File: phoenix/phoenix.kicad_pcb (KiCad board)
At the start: 2 copper layers, 62.7 x 22.6 mm, 2 parts, among them U1 ATMEGA328P-AU

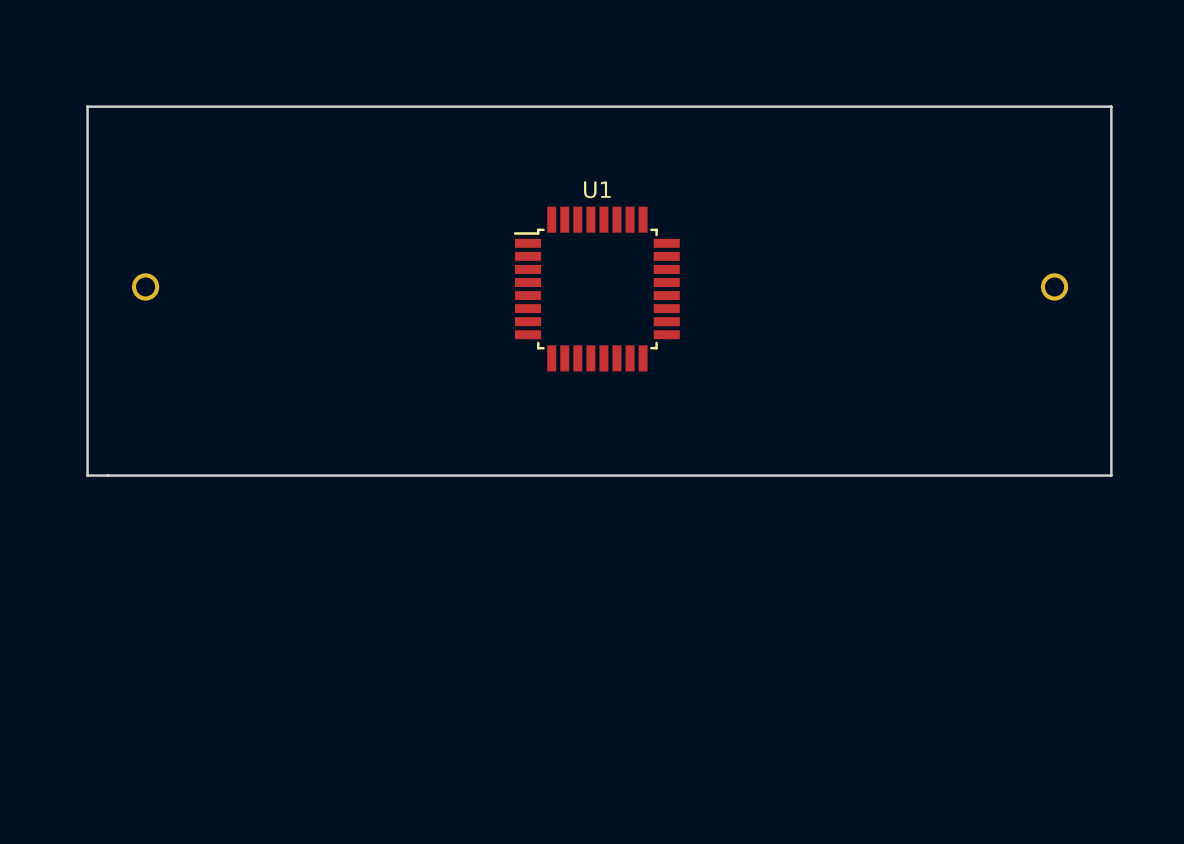
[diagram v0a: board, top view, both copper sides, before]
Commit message: Started layout
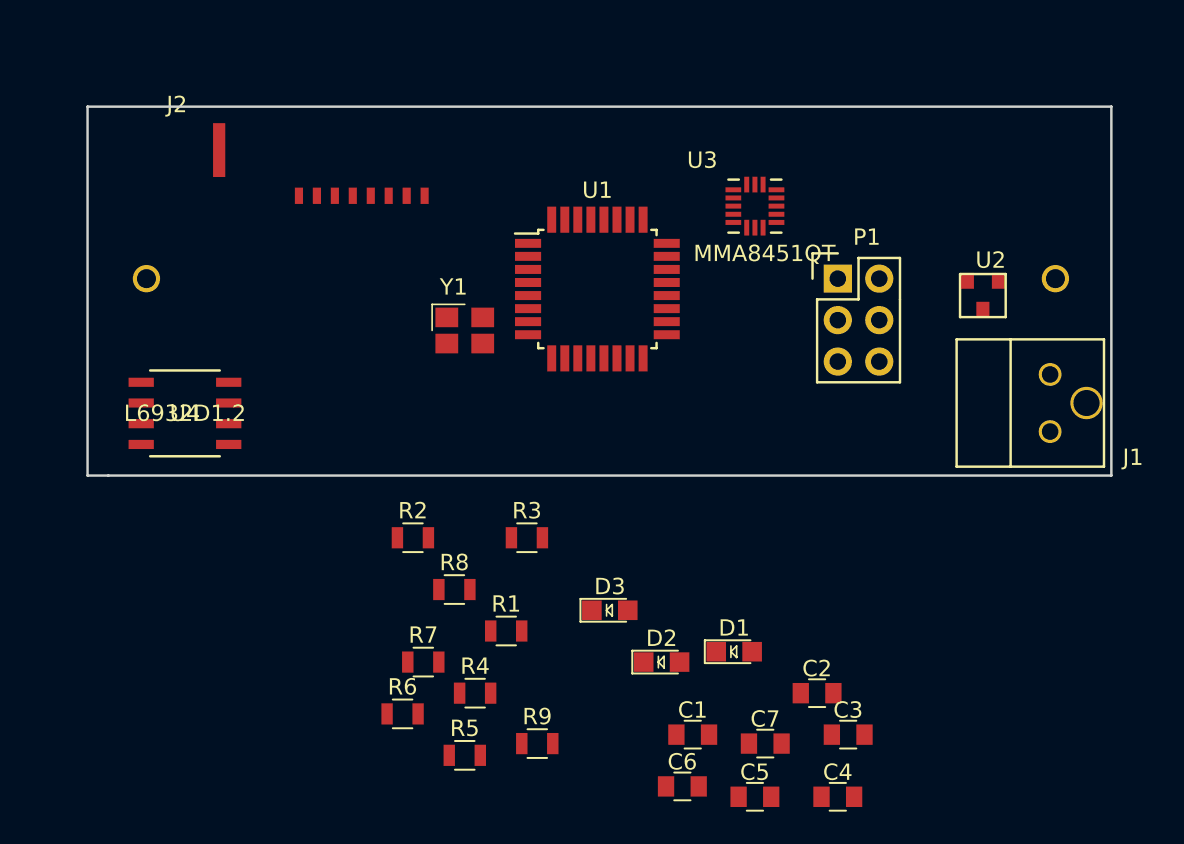
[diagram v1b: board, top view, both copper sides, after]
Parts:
- removed REF**: battery_holder, rocketry:battery_holder
- added BT1: 3.7V Lipo, rocketry:battery_holder, B.Cu at (112.6, 64.1)
- added C1: C_0.1uF, footprints:C_0805_OEM, F.Cu at (146.1, 92.1)
- added C2: C_0.1uF, footprints:C_0805_OEM, F.Cu at (153.7, 89.5)
- added C3: C_10uF, footprints:C_0805_OEM, F.Cu at (155.6, 92.1)
- added C4: C_10uF, footprints:C_0805_OEM, F.Cu at (154.9, 95.9)
- added C5: C_100pF, footprints:C_0805_OEM, F.Cu at (149.9, 95.9)
- added C6: C_30pF, footprints:C_0805_OEM, F.Cu at (145.4, 95.2)
- added C7: C_30pF, footprints:C_0805_OEM, F.Cu at (150.5, 92.6)
- added D1: LED_0805, footprints:LED_0805_OEM, F.Cu at (148.6, 87.0)
- added D2: LED_0805, footprints:LED_0805_OEM, F.Cu at (144.1, 87.6)
- added D3: LED_0805, footprints:LED_0805_OEM, F.Cu at (141.0, 84.5)
- added J1: Ultrafit_2, footprints:Ultrafit_2, F.Cu at (167.9, 70.0)
- added J2: Micro_SD_Card_Det, rocketry:SD-Card, F.Cu at (116.7, 54.6)
- added P1: CONN_02X03, footprints:Pin_Header_Straight_2x03, F.Cu at (154.9, 64.1)
- added R1: R_10k, footprints:R_0805_OEM, F.Cu at (134.6, 85.7)
- added R2: 9K, rocketry:R_0805_OEM, F.Cu at (128.9, 80.0)
- added R3: 5K, rocketry:R_0805_OEM, F.Cu at (135.9, 80.0)
- added R4: R_200, footprints:R_0805_OEM, F.Cu at (132.7, 89.5)
- added R5: R_200, footprints:R_0805_OEM, F.Cu at (132.1, 93.3)
- added R6: R_200, footprints:R_0805_OEM, F.Cu at (128.3, 90.8)
- added R7: R_100, footprints:R_0805_OEM, F.Cu at (129.5, 87.6)
- added R8: R_10k, footprints:R_0805_OEM, F.Cu at (131.4, 83.2)
- added R9: R_10k, footprints:R_0805_OEM, F.Cu at (136.5, 92.6)
- added U2: SI4838DY, rocketry:IRLML6344TRPBFCT-ND, F.Cu at (162.9, 64.3)
- added U3: MMA8451QT, rocketry:MMA8451QT, F.Cu at (149.9, 59.7)
- added U4: L6932D1.2, rocketry:L6932D1.2TR, F.Cu at (114.9, 72.4)
- added Y1: Crystal_SMD, footprints:Crystal_SMD_FA238, F.Cu at (132.1, 67.3)
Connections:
- net /GND renamed GND
- U1 pad 1: Net-(U1-Pad1) -> /INT2
- U1 pad 11: Net-(U1-Pad11) -> /SEPERATE
- U1 pad 14: Net-(U1-Pad14) -> /Spi_config
- U1 pad 15: Net-(U1-Pad15) -> /MOSI
- U1 pad 16: Net-(U1-Pad16) -> /MISO
- U1 pad 17: Net-(U1-Pad17) -> /SCK
- U1 pad 23: Net-(U1-Pad23) -> /PLED1
- U1 pad 24: Net-(U1-Pad24) -> /PLED2
- U1 pad 25: Net-(U1-Pad25) -> /PLED3
- U1 pad 27: Net-(U1-Pad27) -> /SDA
- U1 pad 28: Net-(U1-Pad28) -> /SCL
- U1 pad 29: Net-(U1-Pad29) -> /RESET
- U1 pad 32: Net-(U1-Pad32) -> /INT1
- U1 pad 4: Net-(U1-Pad4) -> +3V3
- U1 pad 6: Net-(U1-Pad6) -> +3V3
- U1 pad 7: Net-(U1-Pad7) -> /PB6
- U1 pad 8: Net-(U1-Pad8) -> /PB7

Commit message: fixed power transistor. Added to layout
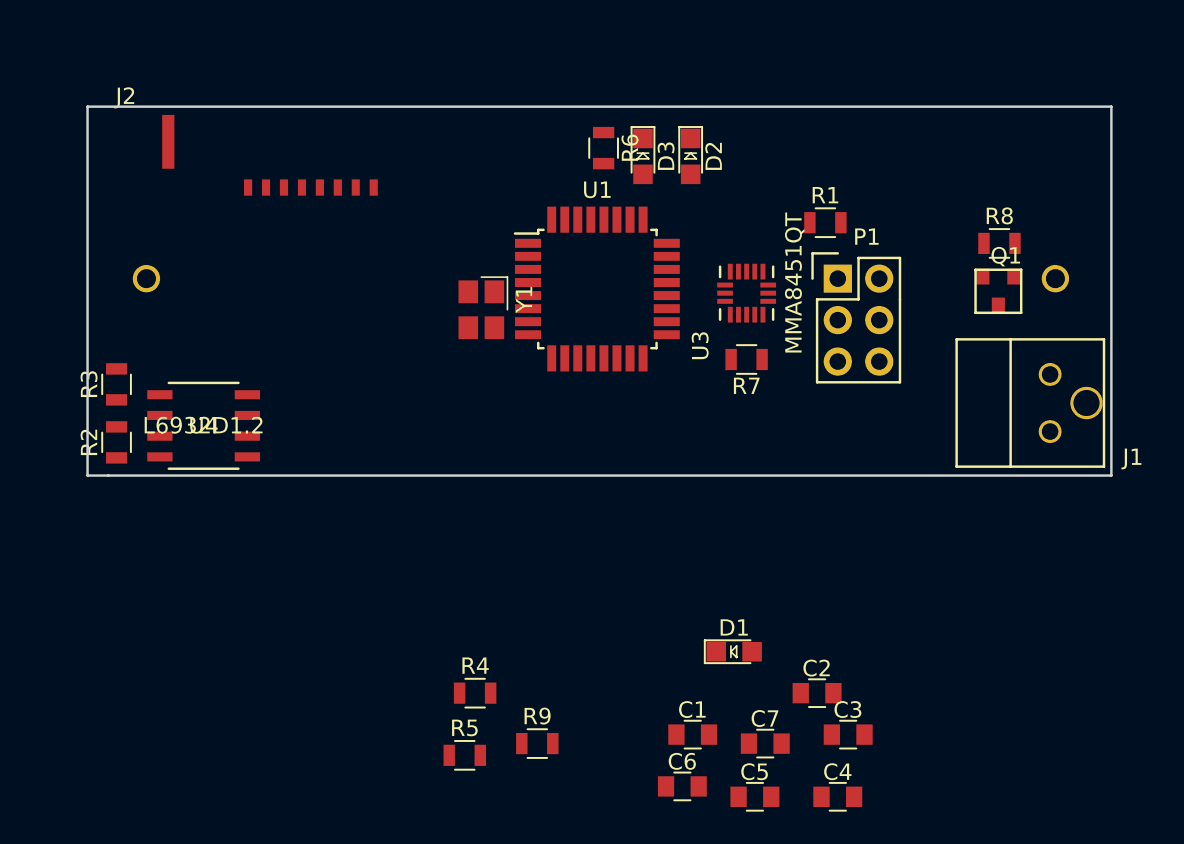
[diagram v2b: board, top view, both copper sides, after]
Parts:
- removed U2: SI4838DY, rocketry:IRLML6344TRPBFCT-ND
- added Q1: IRLML6344, rocketry:IRLML6344TRPBFCT-ND, F.Cu at (163.8, 64.0)
- moved R8 39.6 mm to (164.8, 62.0)
- moved R6 36.8 mm to (140.6, 56.1), turned to 270 degrees
- moved R1 31.8 mm to (154.2, 60.7)
- moved D2 31.0 mm to (145.9, 56.6), turned to 270 degrees
- moved D3 27.9 mm to (143.0, 56.6), turned to 270 degrees
- moved R7 27.1 mm to (149.4, 69.1), turned to 180 degrees
- moved R3 26.8 mm to (110.7, 70.6), turned to 90 degrees
- moved R2 19.1 mm to (110.7, 74.2), turned to 90 degrees
- moved U3 5.36 mm to (149.4, 65.0), turned to 90 degrees
- moved J2 3.16 mm to (113.5, 54.1)
- moved Y1 1.63 mm to (133.1, 66.0), turned to 270 degrees
- moved U4 1.37 mm to (116.1, 73.2)

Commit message: Draft layout
Added:
-changes to layout
-drafted tracing
-modified some footprints
-added 3d-file for micro-sd-card slot
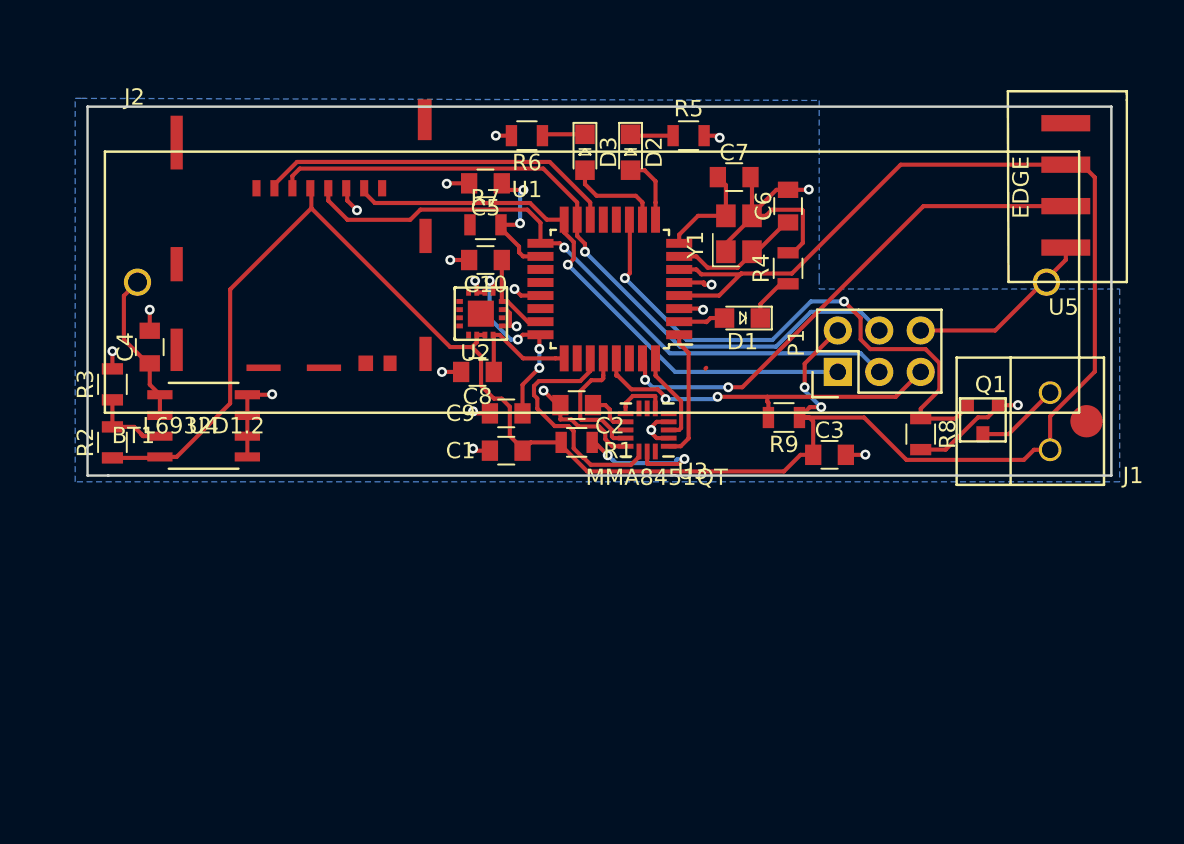
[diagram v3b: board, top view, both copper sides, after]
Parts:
- added C10: C_1000pF, footprints:C_0805_OEM, F.Cu at (133.3, 63.0)
- added C8: C_1000pF, footprints:C_0805_OEM, F.Cu at (132.9, 69.8)
- added C9: C_1000pF, footprints:C_0805_OEM, F.Cu at (134.6, 72.4)
- added U2: ADX377, rocketry:ADXL377, F.Cu at (133.1, 66.3)
- added U5: RFTRANS434MHZ, rocketry:RFTRANS434MHZ, F.Cu at (168.9, 62.2)
- BT1: moved to F.Cu
- moved C4 50.4 mm to (112.8, 68.3), turned to 90 degrees
- moved C5 41.1 mm to (133.3, 58.3), turned to 180 degrees
- moved R5 40.4 mm to (145.8, 55.4)
- moved C6 36.1 mm to (151.9, 59.7), turned to 90 degrees
- moved C7 34.8 mm to (148.6, 57.9)
- moved R4 32.3 mm to (151.9, 63.5), turned to 90 degrees
- moved R9 25.1 mm to (151.6, 72.6), turned to 180 degrees
- moved C2 23.0 mm to (138.9, 71.9), turned to 180 degrees
- moved C1 20.8 mm to (134.6, 74.7), turned to 180 degrees
- moved D1 20.5 mm to (149.1, 66.5), turned to 180 degrees
- moved R1 20.3 mm to (138.9, 74.2), turned to 180 degrees
- moved R7 18.0 mm to (133.3, 60.8), turned to 0 degrees
- moved C3 17.2 mm to (154.4, 74.9)
- moved Y1 16.5 mm to (148.9, 61.4), turned to 90 degrees
- moved R8 12.6 mm to (160.0, 73.7), turned to 270 degrees
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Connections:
- U1 pad 10: Net-(U1-Pad10) -> /PLED3
- U1 pad 2: Net-(U1-Pad2) -> /PLED1
- U1 pad 23: /PLED1 -> /YOUT
- U1 pad 24: /PLED2 -> /XOUT
- U1 pad 25: /PLED3 -> /ZOUT
- U1 pad 31: Net-(U1-Pad31) -> /TX
- U1 pad 9: Net-(U1-Pad9) -> /PLED2
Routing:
- net +3V3: track 0.00 -> 143.9 mm, vias 0 -> 2
- net GND: track 0.00 -> 71.7 mm, vias 0 -> 21
- net /MOSI: track 0.00 -> 44.5 mm, vias 0 -> 1
- net /SCK: track 0.00 -> 40.1 mm, vias 0 -> 1
- net /MISO: track 0.00 -> 35.6 mm, vias 0 -> 1
- net /SEPERATE: track 0.00 -> 35.0 mm, vias 0 -> 2
- net /TX: track 0.00 -> 31.9 mm, vias 0 -> 2
- net /Spi_config: track 0.00 -> 22.5 mm
- net /RESET: track 0.00 -> 22.4 mm, vias 0 -> 2
- net /SDA: track 0.00 -> 14.9 mm
- net /XOUT: track 0.00 -> 12.2 mm, vias 0 -> 4
- net Net-(R1-Pad1): track 0.00 -> 9.93 mm, vias 0 -> 2
- net /VIN: track 0.00 -> 9.50 mm
- net Net-(C5-Pad1): track 0.00 -> 8.46 mm, vias 0 -> 2
- net /PB6: track 0.00 -> 8.17 mm
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- added copper zone on B.Cu, net GND
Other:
- net class Default: clearance 0.2 -> 0.1524; trace_width 0.25 -> 0.254; via_dia 0.6 -> 0.6096; via_drill 0.4 -> 0.3048
- rule trace_clearance: 0.2 -> 0.1524
- rule trace_min: 0.2 -> 0.254
- rule via_min_drill: 0.3 -> 0.3048
- rule via_min_size: 0.4 -> 0.6096

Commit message: Update layout and tracing
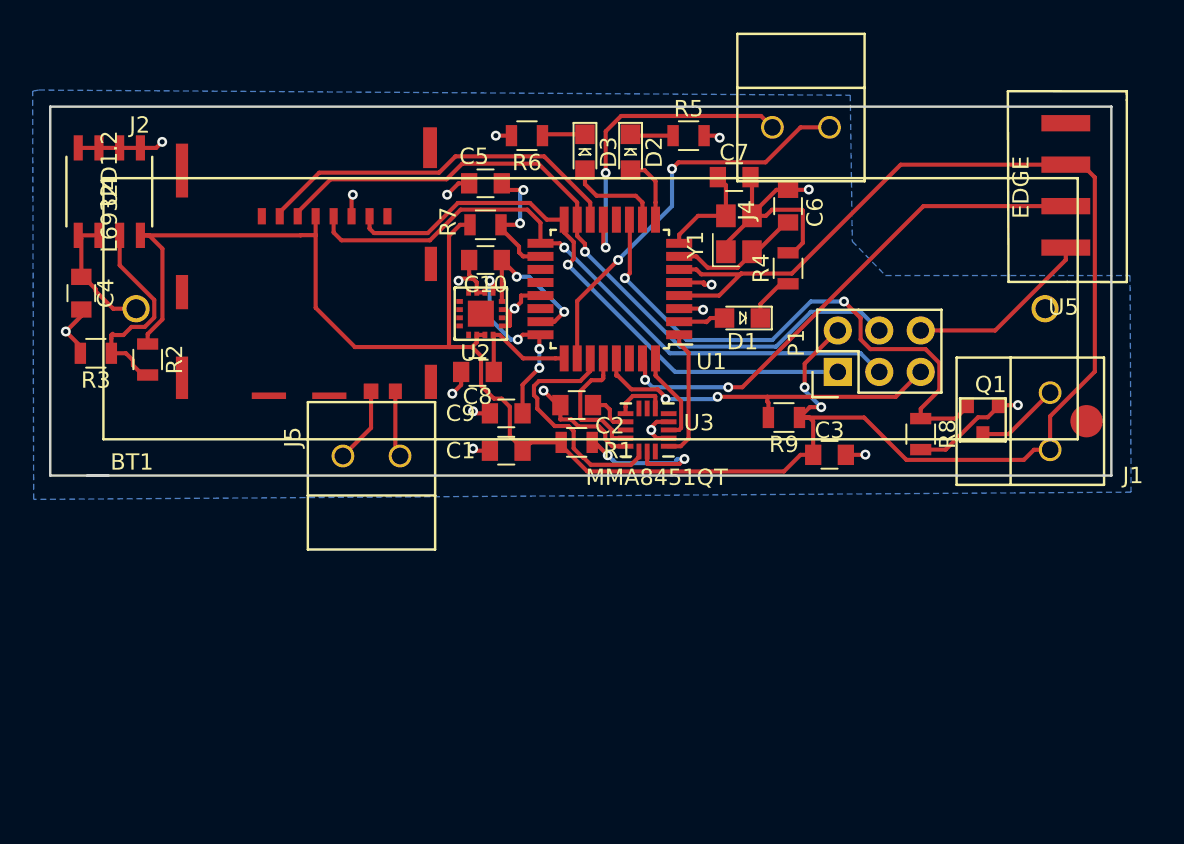
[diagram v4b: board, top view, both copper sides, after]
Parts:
- added J4: Ultrafit_2, footprints:Ultrafit_2, F.Cu at (154.4, 54.9)
- added J5: Ultrafit_2, footprints:Ultrafit_2, F.Cu at (124.6, 75.0)
- moved U4 15.5 mm to (110.3, 58.8), turned to 90 degrees
- moved R2 5.52 mm to (112.6, 69.1), turned to 270 degrees
- moved C4 5.34 mm to (108.6, 65.0), turned to 270 degrees
- moved R3 2.16 mm to (109.5, 68.7), turned to 180 degrees
- moved J2 1.75 mm to (114.4, 55.9)
- moved BT1 1.63 mm to (111.9, 66.0)
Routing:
- net Net-(U1-Pad26): track 0.00 -> 24.7 mm, vias 0 -> 2
- net Net-(U1-Pad13): track 0.00 -> 19.8 mm, vias 0 -> 2
- net Net-(R2-Pad2): track 4.81 -> 13.2 mm
- net +3V3: track 143.9 -> 149.9 mm
- net Net-(J2-Pad9): track 0.00 -> 4.68 mm
- net Net-(J2-Pad10): track 0.00 -> 4.08 mm
- net /YOUT: track 5.41 -> 9.46 mm, vias 0 -> 2
- net GND: track 71.7 -> 75.6 mm, vias 21 -> 18
- net /VIN: track 9.50 -> 8.59 mm
- net /MISO: track 35.6 -> 36.4 mm
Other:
- board size 62.7 x 22.6 mm -> 65 x 22.6 mm

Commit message: Fix references
stuuf
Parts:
- BT1: moved to B.Cu
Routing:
- net /INT1: track 5.73 -> 6.61 mm
- net Net-(R2-Pad2): track 13.2 -> 12.5 mm
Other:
- board text added: "4/16/18"
- board text added: "Corey Cochran-Lepiz"
- board text added: "ORC"
- board text added: "REV_1"
- board text added: "William Fairman"
